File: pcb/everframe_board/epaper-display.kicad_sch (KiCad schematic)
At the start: 1 part, among them J1 62684-501100ALF

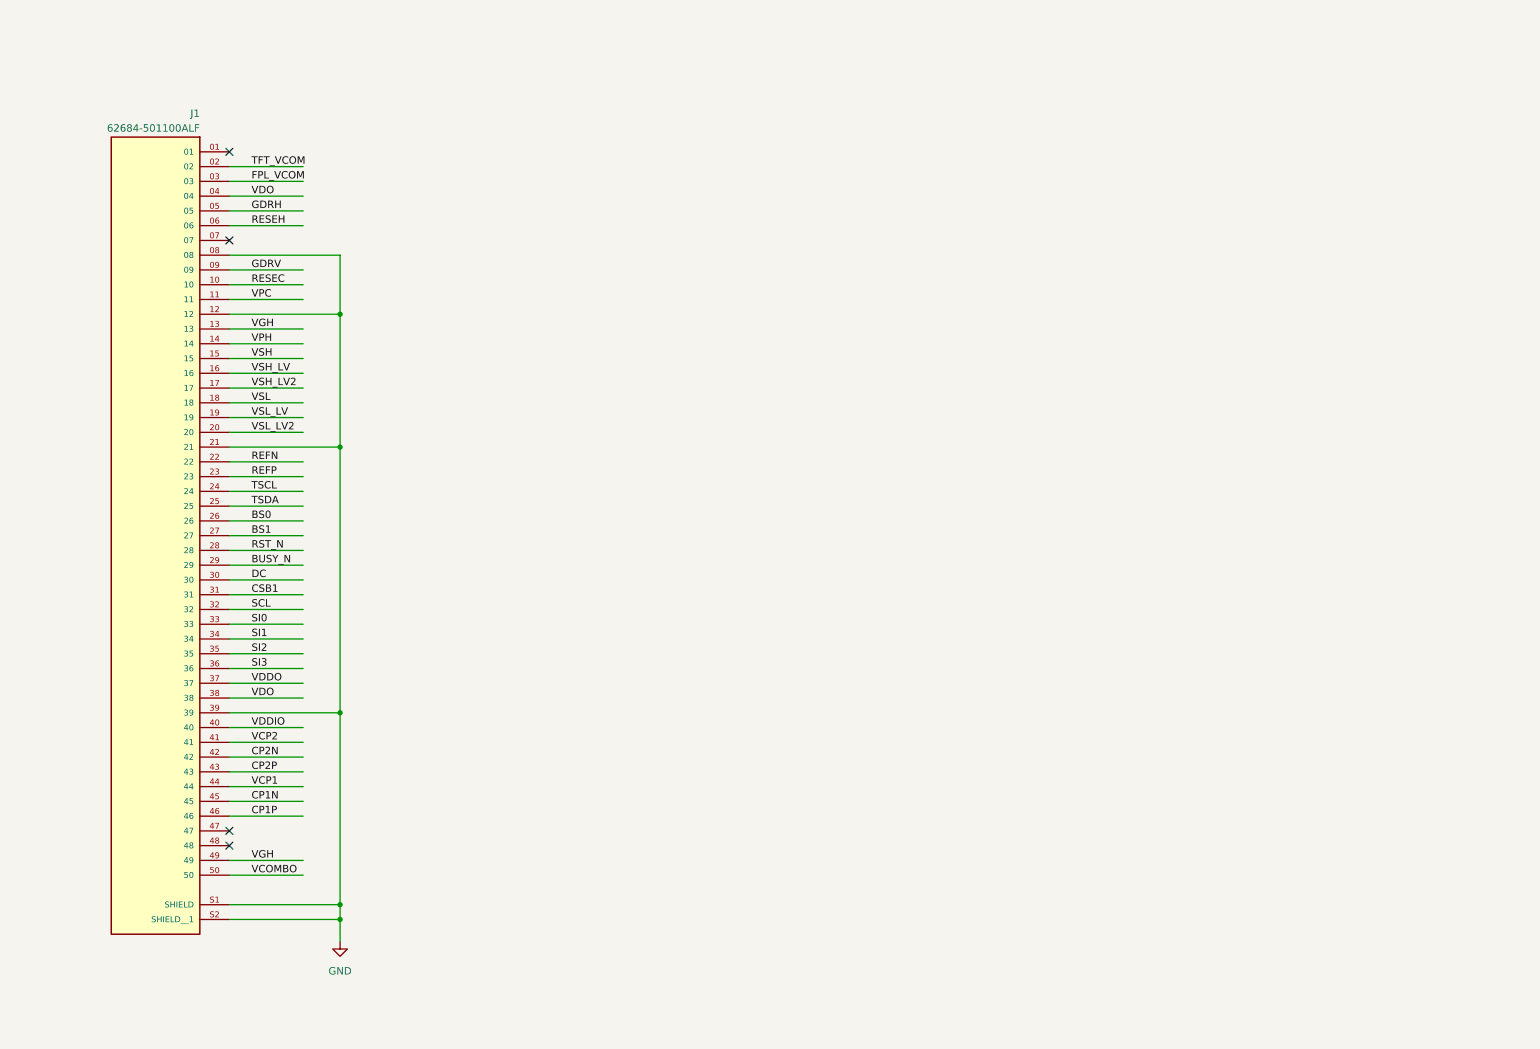
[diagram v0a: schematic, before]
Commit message: Finished sch, started layout 2L only
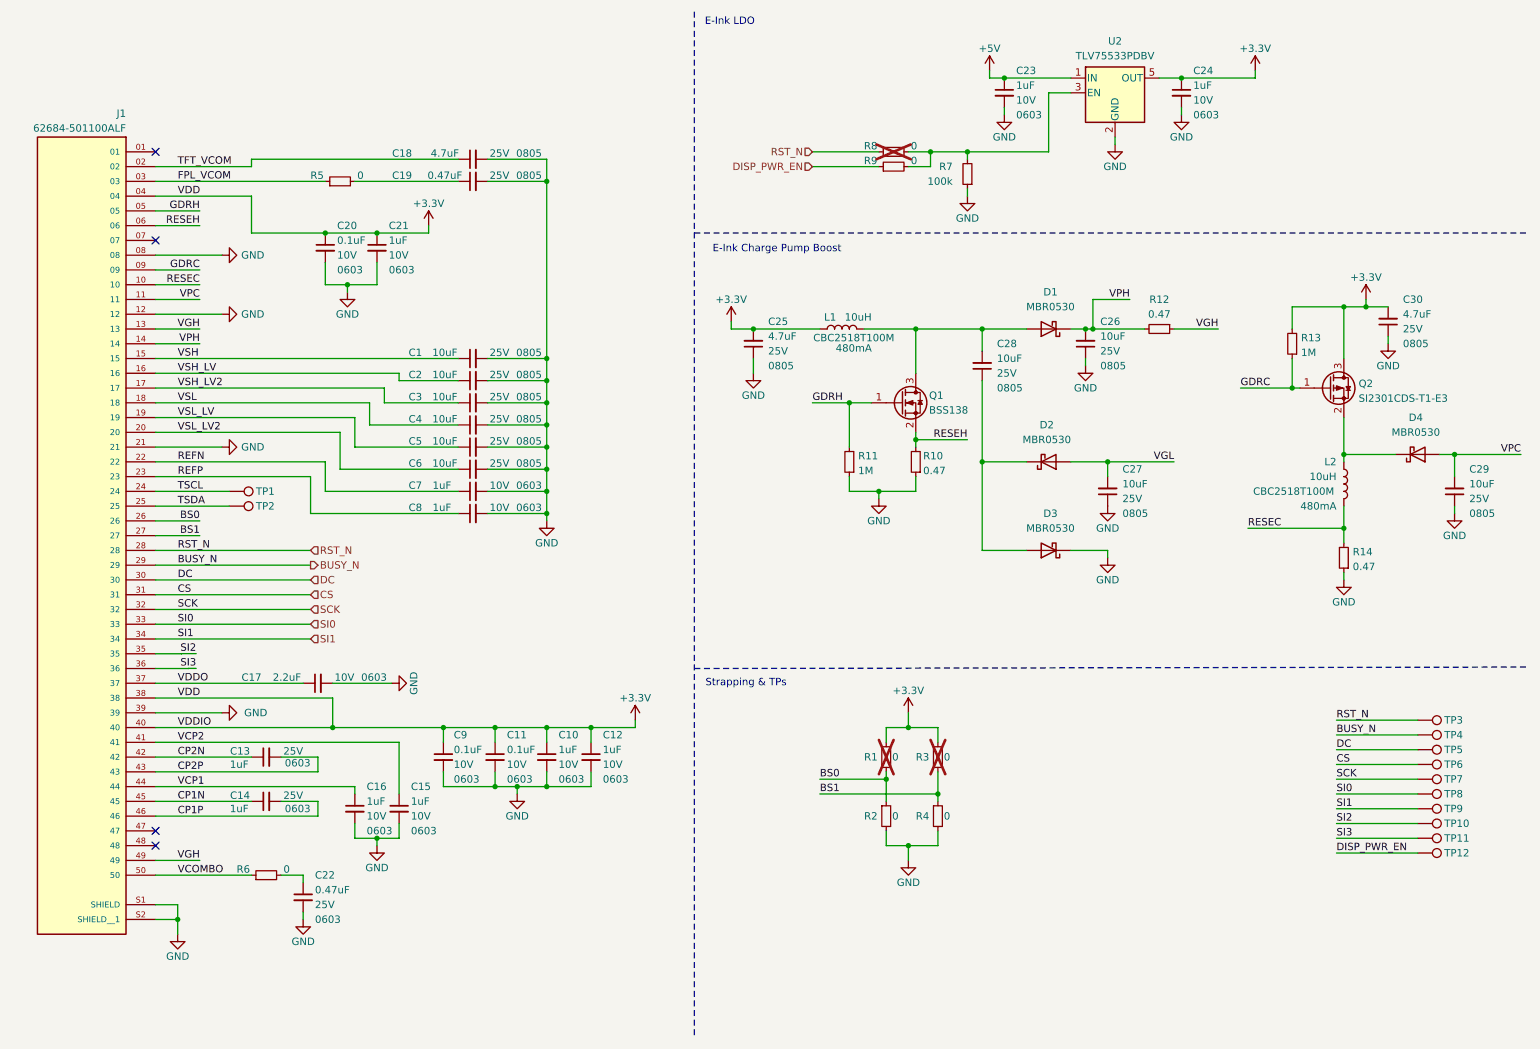
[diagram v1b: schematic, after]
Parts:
- added C1, C2, C26, C27, C28, C29, C3, C4, C5, C6: 10uF, Capacitor_SMD:C_0805_2012Metric, symbol Device:C_Small
- added C10, C12, C13, C14, C15, C16, C21, C23, C24, C7, C8: 1uF, Capacitor_SMD:C_0603_1608Metric, symbol Device:C_Small
- added C11, C20, C9: 0.1uF, Capacitor_SMD:C_0603_1608Metric, symbol Device:C_Small
- added C17: 2.2uF, Capacitor_SMD:C_0603_1608Metric, symbol Device:C_Small
- added C18, C25, C30: 4.7uF, Capacitor_SMD:C_0805_2012Metric, symbol Device:C_Small
- added C19: 0.47uF, Capacitor_SMD:C_0805_2012Metric, symbol Device:C_Small
- added C22: 0.47uF, Capacitor_SMD:C_0603_1608Metric, symbol Device:C_Small
- added D1, D2, D3, D4: MBR0530, Diode_SMD:D_SOD-123, symbol Diode:MBR0530
- added L1, L2: 10uH, Inductor_SMD:L_1008_2520Metric, symbol Device:L
- added Q1: BSS138, Package_TO_SOT_SMD:SOT-23, symbol Transistor_FET:BSS138
- added Q2: SI2301CDS-T1-E3, Package_TO_SOT_SMD:SOT-23, symbol Transistor_FET:Q_PMOS_GSD
- added R1, R2, R3, R4, R5, R6, R8, R9: 0, Resistor_SMD:R_0603_1608Metric, symbol Device:R_Small
- added R10, R12, R14: 0.47, Resistor_SMD:R_0603_1608Metric, symbol Device:R_Small
- added R11, R13: 1M, Resistor_SMD:R_0603_1608Metric, symbol Device:R_Small
- added R7: 100k, Resistor_SMD:R_0603_1608Metric, symbol Device:R_Small
- added TP1, TP10, TP11, TP12, TP2, TP3, TP4, TP5, TP6, TP7, TP8, TP9: TestPoint, TestPoint:TestPoint_Pad_2.0x2.0mm, symbol Connector:TestPoint
- added U2: TLV75533PDBV, Package_TO_SOT_SMD:SOT-23-5, symbol Regulator_Linear:TLV75533PDBV
- J1: footprint 62684-501100ALF:AMPHENOL_62684-501100ALF -> everframe_library.footprints:AMPHENOL_62684-501100ALF
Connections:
- net VDO is gone; now on net +3.3V: J1.04, J1.38
- net BS0: now also R1.2, R2.1
- net BS1: now also R3.2, R4.1
- net BUSY_N: now also TP4.1
- net CP1N: now also C14.1
- net CP1P: now also C14.2
- net CP2N: now also C13.1
- net CP2P: now also C13.2
- net DC: now also TP5.1
- net FPL_VCOM: now also R5.1
- net GDRH: now also Q1.1 (G), R11.2
- net GND: now also C1.2, C10.2, C11.2, C12.2, C15.2, C16.2, C17.2, C18.2, C19.2, C2.2, C20.2, C21.2, C22.2, C23.2, C24.2, C25.1, C26.1, C27.1, C29.1, C3.2, C30.1, C4.2, C5.2, C6.2, C7.2, C8.2, C9.2, D3.1 (K), R10.1, R11.1, R14.1, R2.2, R4.2, R7.1, U2.2 (GND)
- net REFN: now also C7.1
- net REFP: now also C8.1
- net RESEC: now also L2.1, R14.2
- net RESEH: now also Q1.2 (S), R10.2
- net RST_N: now also R8.1, TP3.1
- net SI0: now also TP8.1
- net SI1: now also TP9.1
- net SI2: now also TP10.1
- net SI3: now also TP11.1
- net TFT_VCOM: now also C18.1
- net TSCL: now also TP1.1
- net TSDA: now also TP2.1
- net VCOMBO: now also R6.1
- net VCP1: now also C16.1
- net VCP2: now also C15.1
- net VDDO: now also C17.1
- net VGH: now also R12.1
- net VPC: now also C29.2, D4.2 (A)
- net VPH: now also C26.2, D1.1 (K), R12.2
- net VSH: now also C1.1
- net VSH_LV: now also C2.1
- net VSH_LV2: now also C3.1
- net VSL: now also C4.1
- net VSL_LV: now also C5.1
- net VSL_LV2: now also C6.1
- net CSB1 renamed CS
- net CS: now also TP6.1
- net GDRV renamed GDRC
- net GDRC: now also Q2.1 (G), R13.1
- net SCL renamed SCK
- net SCK: now also TP7.1
- net VDDIO renamed +3.3V
- net +3.3V: now also C10.1, C11.1, C12.1, C20.1, C21.1, C24.1, C25.2, C30.2, C9.1, L1.1, Q2.3 (D), R1.1, R13.2, R3.1, U2.5 (OUT)
- new net: R7.2, R8.2, R9.2, U2.3 (EN)
- new net: C28.2, D1.2 (A), L1.2, Q1.3 (D)
- new net: C28.1, D2.1 (K), D3.2 (A)
- new net: C22.1, R6.2
- new net: D4.1 (K), L2.2, Q2.2 (S)
- new net: C19.1, R5.2
- new net +5V: C23.1, U2.1 (IN)
- new net DISP_PWR_EN: R9.1, TP12.1
- new net VGL: C27.2, D2.2 (A)
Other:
- note added: "E-Ink Charge Pump Boost"
- note added: "E-Ink LDO"
- note added: "Strapping & TPs"
- moved on the sheet: J1

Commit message: Routed board, mostly need checks
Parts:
- removed TP1, TP10, TP11, TP12, TP2, TP3, TP4, TP5, TP6, TP7, TP8, TP9: TestPoint, TestPoint:TestPoint_Pad_2.0x2.0mm, symbol Connector:TestPoint
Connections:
- net VGH: no longer J1.13
- net VGL: now also J1.13
- net TSCL: no longer names the net of J1.24
- net TSDA: no longer names the net of J1.25
- no-connect marks 4 -> 6
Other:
- note added: "Strapping"
- note removed: "Strapping & TPs"

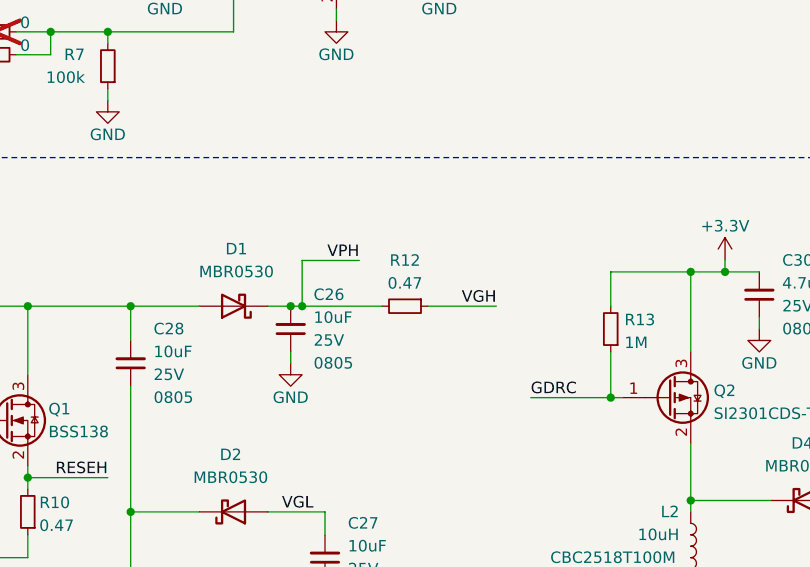
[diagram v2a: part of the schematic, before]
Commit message: Some unused google cloud function code added, esp32 idf embedded project added with display drivers, pcb fab exported
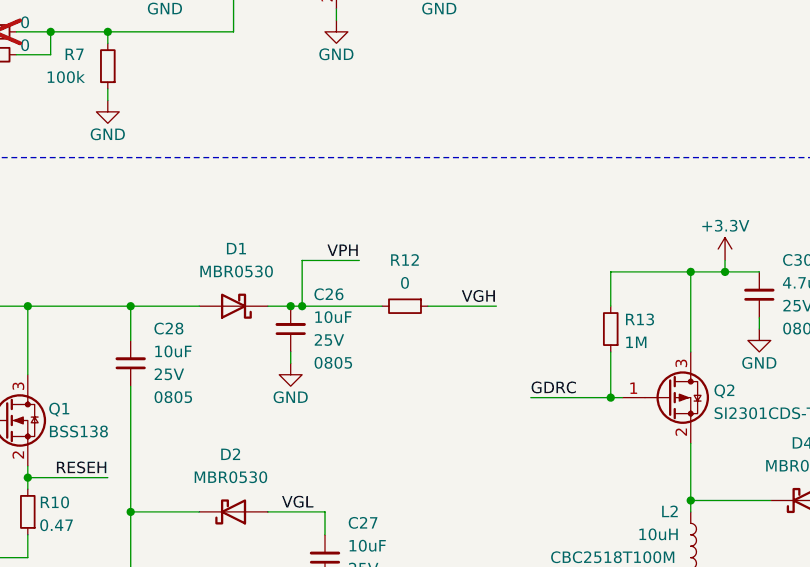
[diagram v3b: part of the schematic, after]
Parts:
- R12: value 0.47 -> 0
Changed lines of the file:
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@@
 	(title_block
 		(title "Everframe Mainboard")
-		(rev "0.0.1")
+		(date "2025-11-24")
+		(rev "1.0.0")
 	)
 	(text "E-Ink LDO"
@@
 			)
 		)
-		(property "Value" "0.47"
+		(property "Value" "0"
 			(at 219.71 64.77 90)
 			(effects
